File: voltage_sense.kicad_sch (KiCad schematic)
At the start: 11 parts, among them U6 24AA025UID, U9 LP2981A-33DBVT

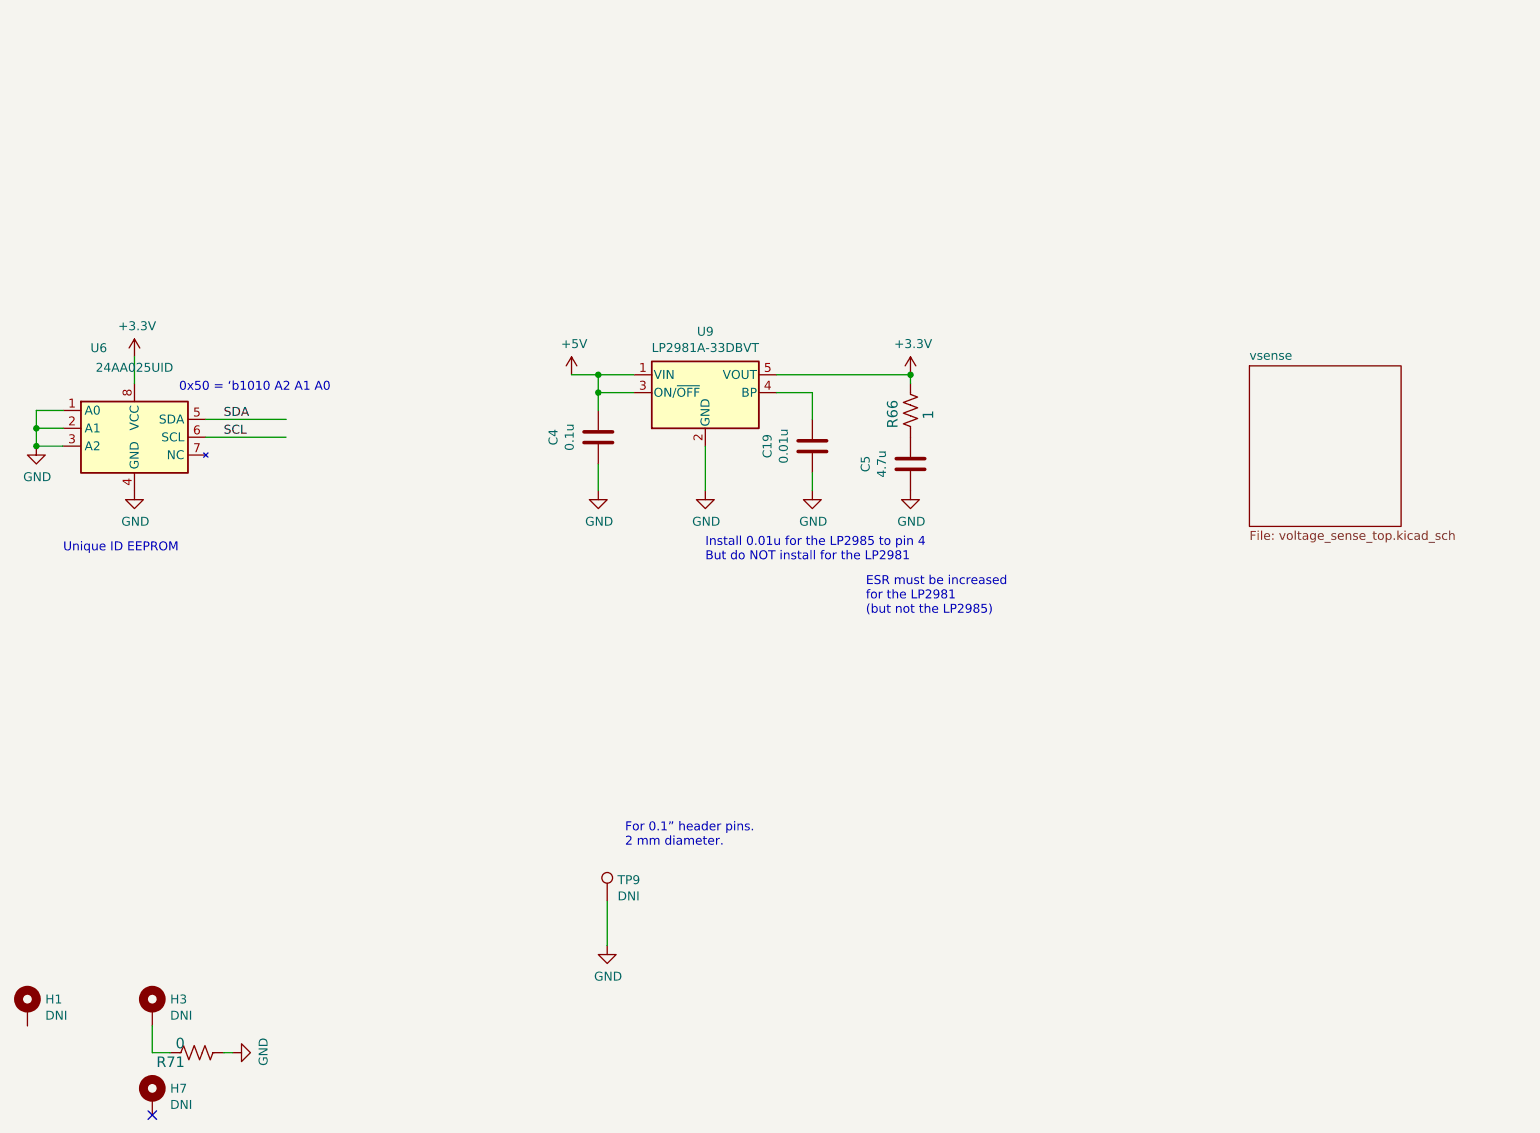
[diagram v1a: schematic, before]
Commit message: moved SMA to same size as HDMI
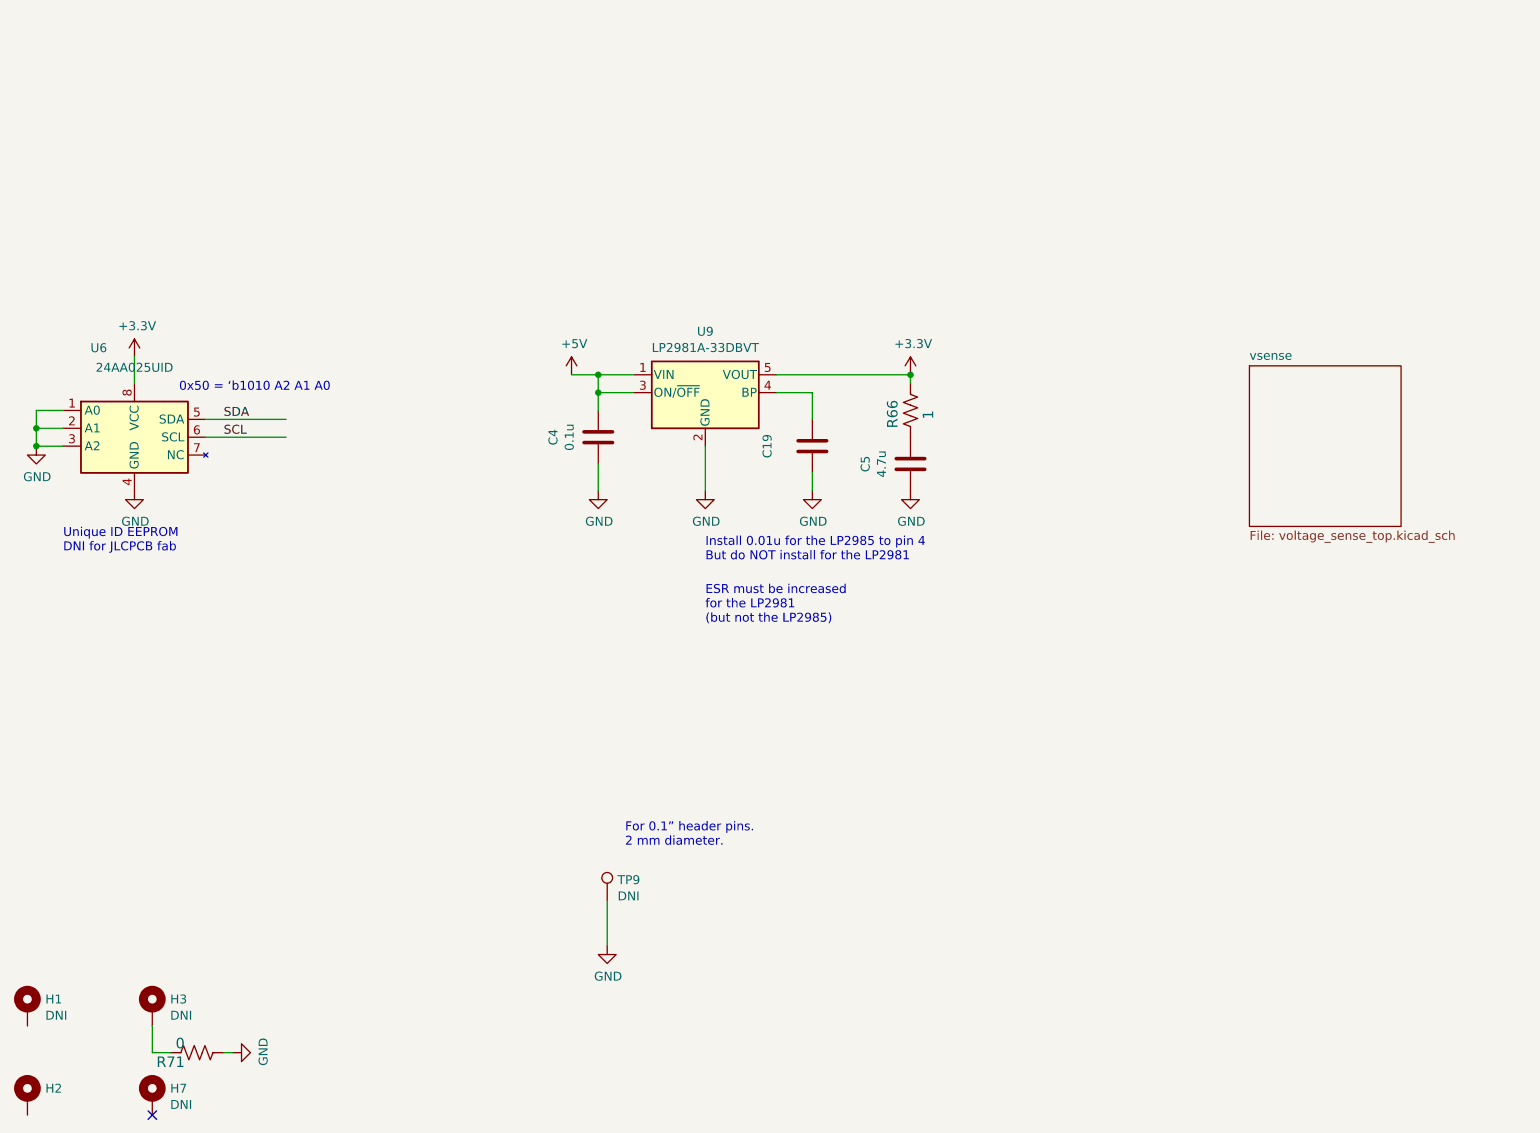
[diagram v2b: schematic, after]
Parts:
- added H2: (no value), symbol Mechanical:MountingHole_Pad
- C19: value 0.01u -> (none); footprint Capacitor_SMD:C_0603_1608Metric -> (none); Manf# CC0603MRX7R8BB103 -> (none); Tolerance 20% -> (none); voltage 25V -> (none)
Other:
- note added: "Unique ID EEPROM DNI for JLCPCB fab"
- note removed: "Unique ID EEPROM"
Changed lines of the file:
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@@
     (effects (font (size 1.27 1.27)) (justify left bottom))
   )
-  (text "Unique ID EEPROM" (at 35.56 109.22 0)
+  (text "Unique ID EEPROM\nDNI for JLCPCB fab" (at 35.56 109.22 0)
     (effects (font (size 1.27 1.27)) (justify left bottom))
   )
@@
   )
   (text "ESR must be increased \nfor the LP2981\n(but not the LP2985)"
-    (at 149.86 118.11 0)
+    (at 127 119.38 0)
     (effects (font (size 1.27 1.27)) (justify left bottom))
   )
@@
     (in_bom yes) (on_board yes)
     (property "Reference" "C19" (id 0) (at 135.8392 93.98 90))
-    (property "Value" "0.01u" (id 1) (at 138.1506 93.98 90))
-    (property "Footprint" "Capacitor_SMD:C_0603_1608Metric" (id 2) (at 143.2052 97.79 0)
+    (property "Value" "" (id 1) (at 138.1506 93.98 90))
+    (property "Footprint" "" (id 2) (at 143.2052 97.79 0)
       (effects (font (size 1.27 1.27)) hide)
     )
@@
       (effects (font (size 1.27 1.27)) hide)
     )
-    (property "Manf#" "CC0603MRX7R8BB103" (id 4) (at 135.8392 91.44 0)
-      (effects (font (size 1.27 1.27)) hide)
-    )
-    (property "Tolerance" "20%" (id 5) (at 135.8392 91.44 0)
-      (effects (font (size 1.27 1.27)) hide)
-    )
-    (property "voltage" "25V" (id 6) (at 135.8392 91.44 0)
+    (property "Manf#" "~" (id 4) (at 135.8392 91.44 0)
+      (effects (font (size 1.27 1.27)) hide)
+    )
+    (property "Tolerance" "~" (id 5) (at 135.8392 91.44 0)
+      (effects (font (size 1.27 1.27)) hide)
+    )
+    (property "voltage" "~" (id 6) (at 135.8392 91.44 0)
       (effects (font (size 1.27 1.27)) hide)
     )
@@
     (pin "1")
   )
+  (symbol (lib_id "Mechanical:MountingHole_Pad") (at 30.48 186.69 0) (unit 1)
+    (in_bom yes) (on_board yes)
+    (property "Reference" "H2" (id 0) (at 33.02 185.4454 0)
+      (effects (font (size 1.27 1.27)) (justify left))
+    )
+    (property "Value" "" (id 1) (at 33.02 187.7568 0)
+      (effects (font (size 1.27 1.27)) (justify left))
+    )
+    (property "Footprint" "" (id 2) (at 30.48 186.69 0)
+      (effects (font (size 1.27 1.27)) hide)
+    )
+    (property "Datasheet" "~" (id 3) (at 30.48 186.69 0)
+      (effects (font (size 1.27 1.27)) hide)
+    )
+    (pin "1")
+  )
   (symbol (lib_id "Mechanical:MountingHole_Pad") (at 30.48 173.99 0) (unit 1)
     (in_bom yes) (on_board yes)
@@
     )
     (path "/00000000-0000-0000-0000-0000624cc861"
-      (reference "C19") (unit 1) (value "0.01u") (footprint "Capacitor_SMD:C_0603_1608Metric")
+      (reference "C19") (unit 1) (value "DNI") (footprint "Capacitor_SMD:C_0603_1608Metric")
     )
     (path "/8f6452a4-f576-403e-b12d-634ebe6e21d1/00000000-0000-0000-0000-000061e15819"
@@
       (reference "H1") (unit 1) (value "DNI") (footprint "MountingHole:MountingHole_2.2mm_M2")
     )
+    (path "/62b05cc2-d33e-48a4-b819-5e122810ce5b"
+      (reference "H2") (unit 1) (value "DNI") (footprint "MountingHole:MountingHole_2.2mm_M2")
+    )
     (path "/04a87f38-3efc-4636-9bff-903cb1f9cad3"

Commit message: Add files via upload
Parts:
- added C22: 0.1u, Capacitor_SMD:C_0603_1608Metric, symbol Device:C
- added C23: 1u, Capacitor_SMD:C_0603_1608Metric, symbol Device:C
- added U11: REF3440TIDBVR, covg-kicad:REF3440, symbol REF3440:REF3440TIDBVR
- C19: value (none) -> DNI; footprint (none) -> Capacitor_SMD:C_0603_1608Metric
- H2: value (none) -> DNI; footprint (none) -> MountingHole:MountingHole_2.2mm_M2
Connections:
- net +5V: now also C22.1, U11.3 (ENABLE), U11.4 (IN)
- net GND: now also C22.2, C23.1, U11.1 (GND_F), U11.2 (GND_S)
- net SCL: now also U6.5 (SDA); no longer U6.6 (SCL)
- net SDA: now also U6.6 (SCL); no longer U6.5 (SDA)
- new net +4V: C23.2, U11.5 (OUT_S), U11.6 (OUT_F)
- no-connect marks 1 -> 3
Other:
- note added: "4.096VREF Output (10mA max)"

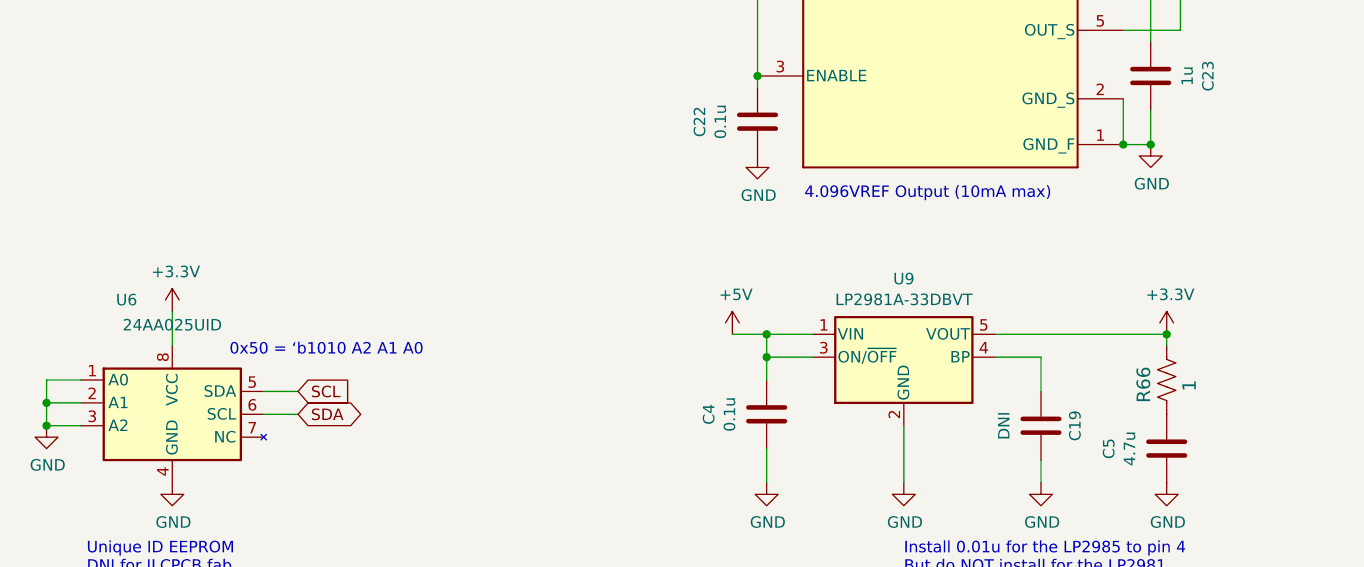
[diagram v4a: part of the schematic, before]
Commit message: add modified production files; schematic update by KiCAD version to 8.0.1
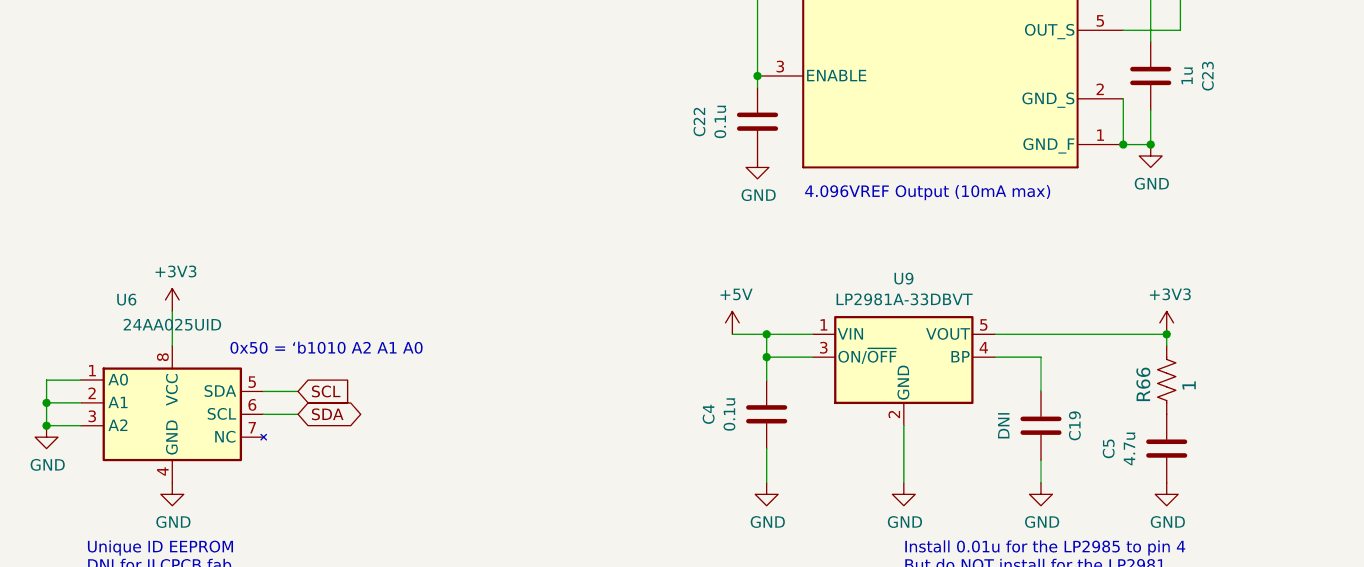
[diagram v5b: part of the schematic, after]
